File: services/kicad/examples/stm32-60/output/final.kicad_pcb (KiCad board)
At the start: 2 copper layers, 132 x 99 mm, 60 parts, among them J1 5V, U1 STM32F103C8T6, U2 AMS1117-3.3

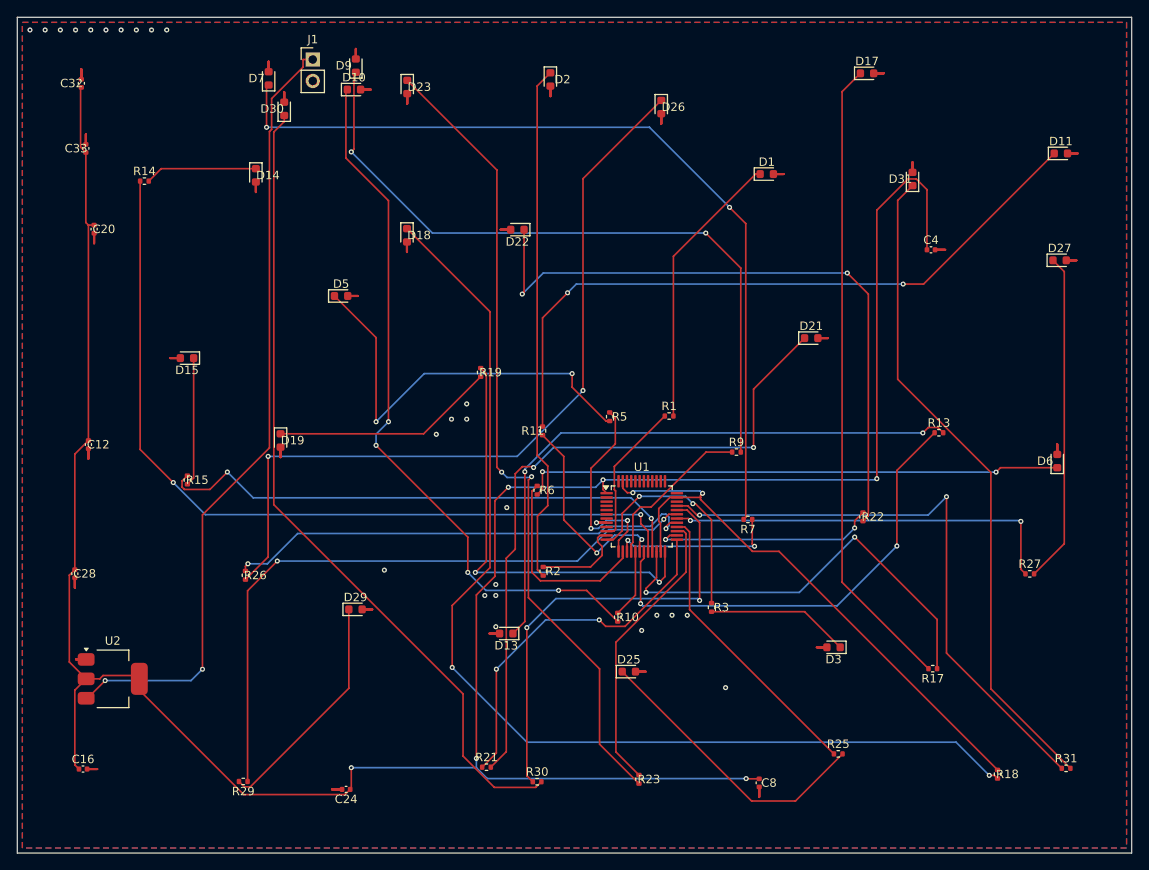
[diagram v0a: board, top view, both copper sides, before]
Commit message: feat(kicad): placement pro et routage 100 % fabricable sur les 16 cartes -- integration sur main (#164)
Branche d'integration coupee depuis origin/main (fab2a82, PR #162) : les
fichiers cles de main etaient des instantanes de feat/placement-seed-snap-
bypass (routing.py = 7981019, placement.py = 437a8b4...). On reprend donc
l'arbre entier de cette branche (345 commits, dernier 9f48667) et on y
conserve ce que main seul apportait :
- tools/verrou_routage.py + son test : « 6,2 Go par routage » rectifie
  (0,2 Go mesure ; c'est la concurrence qui emballe la memoire) ;
- tests/test_driver_llm_resync.py ;
- CLAUDE.md, PLAN.md, DECISIONS.md : fusion a trois voies, les sections
  des deux lignes conservees (2026-09-05 conteneur/verrou, 2026-09-07
  parcours asynchrone et chaine du driver, 2026-09-09/10 lecons).
Les skills *-delegate restent supprimes (remplaces le 2026-08-30).

Contenu : banc en deux phases (placement valide puis routage gele), snap
sur les regles natives, repli GND cible, journal Freerouting incremental,
horloge sans progres, via d'echappement vers le plan principal,
serigraphie degagee ; 16 cartes livrees a 100 %, 0 erreur DRC.

Verification : pytest services/kicad 1805 passed, 16 skipped ;
pnpm type-check 8/8.


Claude-Session: https://claude.ai/code/session_01TnMqm4La2CxQHHB5K8aSSV

Co-authored-by: Claude Fable 5.1 <noreply@anthropic.com>
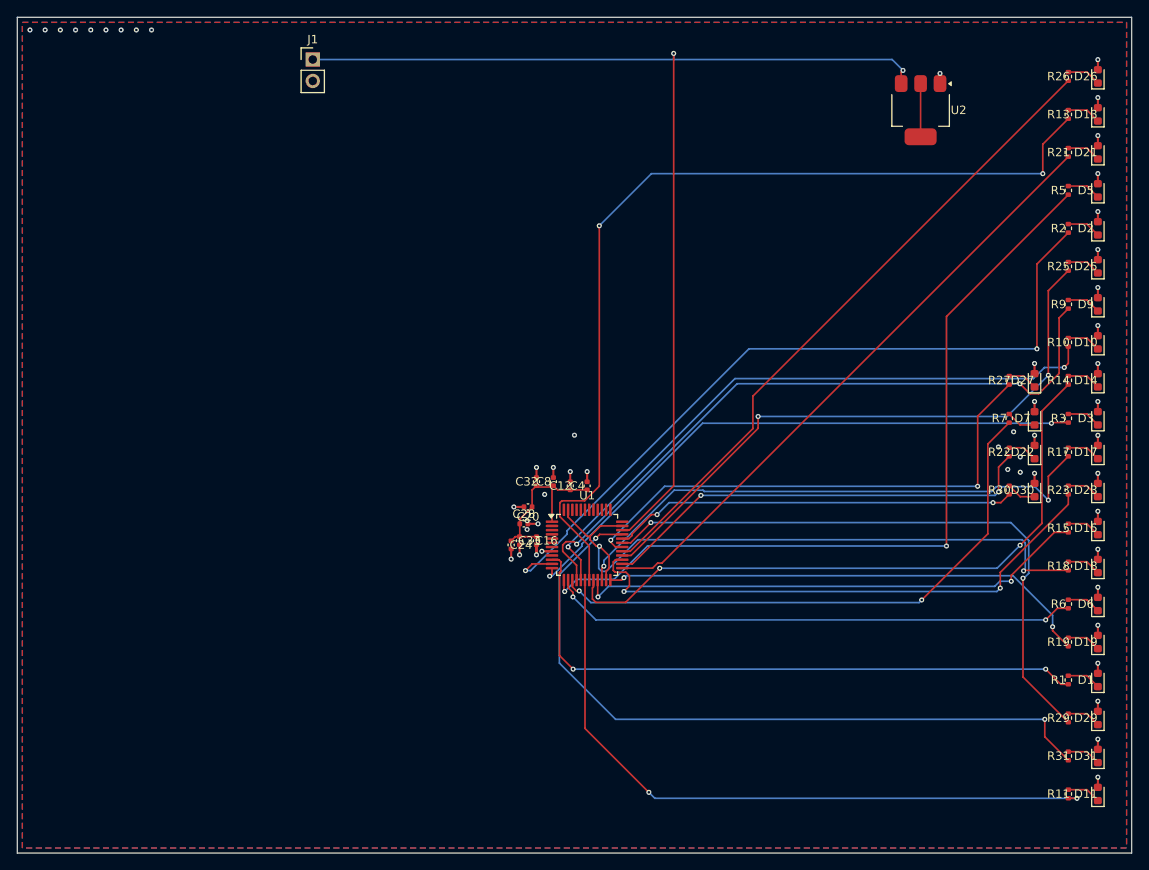
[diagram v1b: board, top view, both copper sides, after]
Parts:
- moved U2 117.0 mm to (189.5, 66.5), turned to -90 degrees
- moved R26 114.0 mm to (207.0, 62.5), turned to 90 degrees
- moved R14 112.0 mm to (207.0, 98.5), turned to 90 degrees
- moved D15 109.8 mm to (210.5, 116.0), turned to 90 degrees
- moved R15 104.5 mm to (207.0, 116.0), turned to 90 degrees
- moved D14 102.7 mm to (210.5, 98.5), turned to 90 degrees
- moved R21 100.3 mm to (207.0, 71.5), turned to 90 degrees
- moved D19 99.7 mm to (210.5, 129.5), turned to 90 degrees
- moved D30 99.7 mm to (203.0, 111.5)
- moved D7 99.3 mm to (203.0, 103.0)
- moved R29 98.0 mm to (207.0, 138.5), turned to 90 degrees
- moved D23 94.7 mm to (210.5, 111.5), turned to 90 degrees
- moved D13 93.2 mm to (210.5, 67.0), turned to 90 degrees
- moved D10 93.1 mm to (210.5, 94.0), turned to 90 degrees
- moved D9 92.3 mm to (210.5, 89.5)
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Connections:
- C12 pad 1: +3.3V -> +3V3
- C16 pad 1: +3.3V -> +3V3
- C20 pad 1: +3.3V -> +3V3
- C24 pad 1: +3.3V -> +3V3
- C28 pad 1: +3.3V -> +3V3
- C32 pad 1: +3.3V -> +3V3
- C33 pad 1: +3.3V -> +3V3
- C4 pad 1: +3.3V -> +3V3
- C8 pad 1: +3.3V -> +3V3
- U1 pad 1: +3.3V -> +3V3
- U1 pad 34: Net-(U1-34) -> VIN
- U2 pad 2: +3.3V -> Net-(U2-2)
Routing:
- net +3.3V: track 301.7 -> 0.00 mm, vias 6 -> 0
- net LED18: track 128.0 -> 4.04 mm, vias 2 -> 0
- net LED7: track 101.8 -> 3.54 mm, vias 2 -> 0
- net LED30: track 96.8 -> 3.54 mm
- net LED23: track 96.8 -> 4.04 mm, vias 2 -> 0
- net LED26: track 94.4 -> 4.04 mm, vias 2 -> 0
- net GND: track 126.0 -> 44.4 mm, vias 26 -> 53
- net LED10: track 84.6 -> 4.04 mm, vias 4 -> 0
- net GPIO2: track 11.0 -> 90.5 mm, vias 0 -> 2
- net LED9: track 83.3 -> 4.04 mm, vias 2 -> 0
- net LED11: track 81.6 -> 4.04 mm, vias 2 -> 0
- net LED21: track 81.0 -> 4.04 mm, vias 2 -> 0
- net LED22: track 77.9 -> 3.54 mm, vias 2 -> 0
- net LED31: track 78.2 -> 4.04 mm
- net GPIO5: track 24.1 -> 96.5 mm
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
